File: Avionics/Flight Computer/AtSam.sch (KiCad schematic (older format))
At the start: 41 parts, among them U12 ATSAME70Q21A-AN, Y1 9HT11-32.768KDZB-T, Y2 7V-16.000MAHJ-T

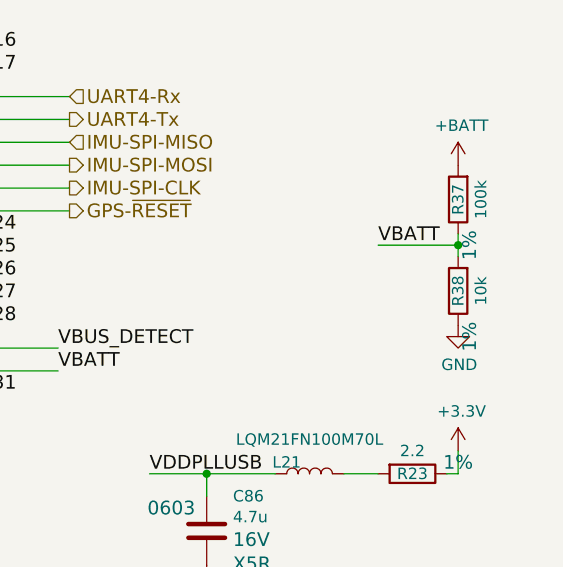
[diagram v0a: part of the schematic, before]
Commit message: Continuing to route out MCU signals.
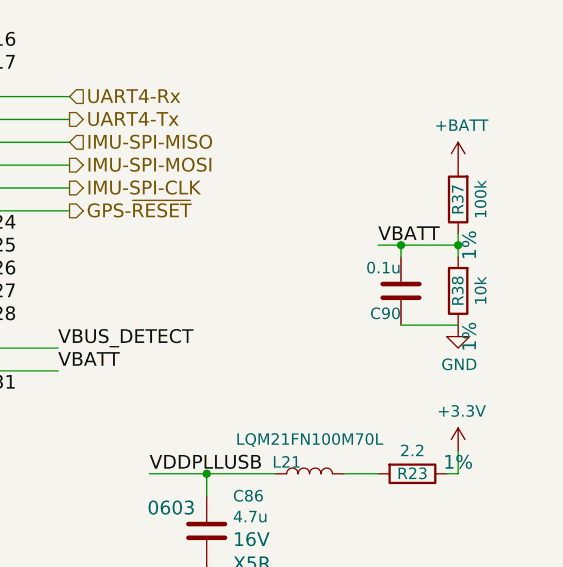
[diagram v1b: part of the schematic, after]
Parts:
- added C90: 0.1u, Capacitors_SMD:C_0402, symbol C
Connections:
- net GND: now also C90.2
- net VBATT: now also C90.1
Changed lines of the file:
@@
 	10850 3900 10850 4000
 Connection ~ 10850 3950
+$Comp
+L C C90
+U 1 1 58BBD62D
+P 10600 4150
+F 0 "C90" H 10600 4050 50  0000 R CNN
+F 1 "0.1u" H 10600 4250 50  0000 R CNN
+F 2 "Capacitors_SMD:C_0402" H 5888 2700 50  0001 C CNN
+F 3 "" H 5850 2850 50  0001 C CNN
+F 4 "50V" H 10485 4188 60  0001 R CNN "Voltage"
+F 5 "20%" H 10715 4006 60  0001 L CNN "Tolerance"
+F 6 "X7R" H 10485 4294 60  0001 R CNN "Type"
+F 7 "0402" H 10715 3953 60  0001 L CNN "Package"
+	1    10600 4150
+	1    0    0    -1
+$EndComp
+Wire Wire Line
+	10600 4000 10600 3950
+Connection ~ 10600 3950
+Wire Wire Line
+	10600 4300 10850 4300
 $EndSCHEMATC

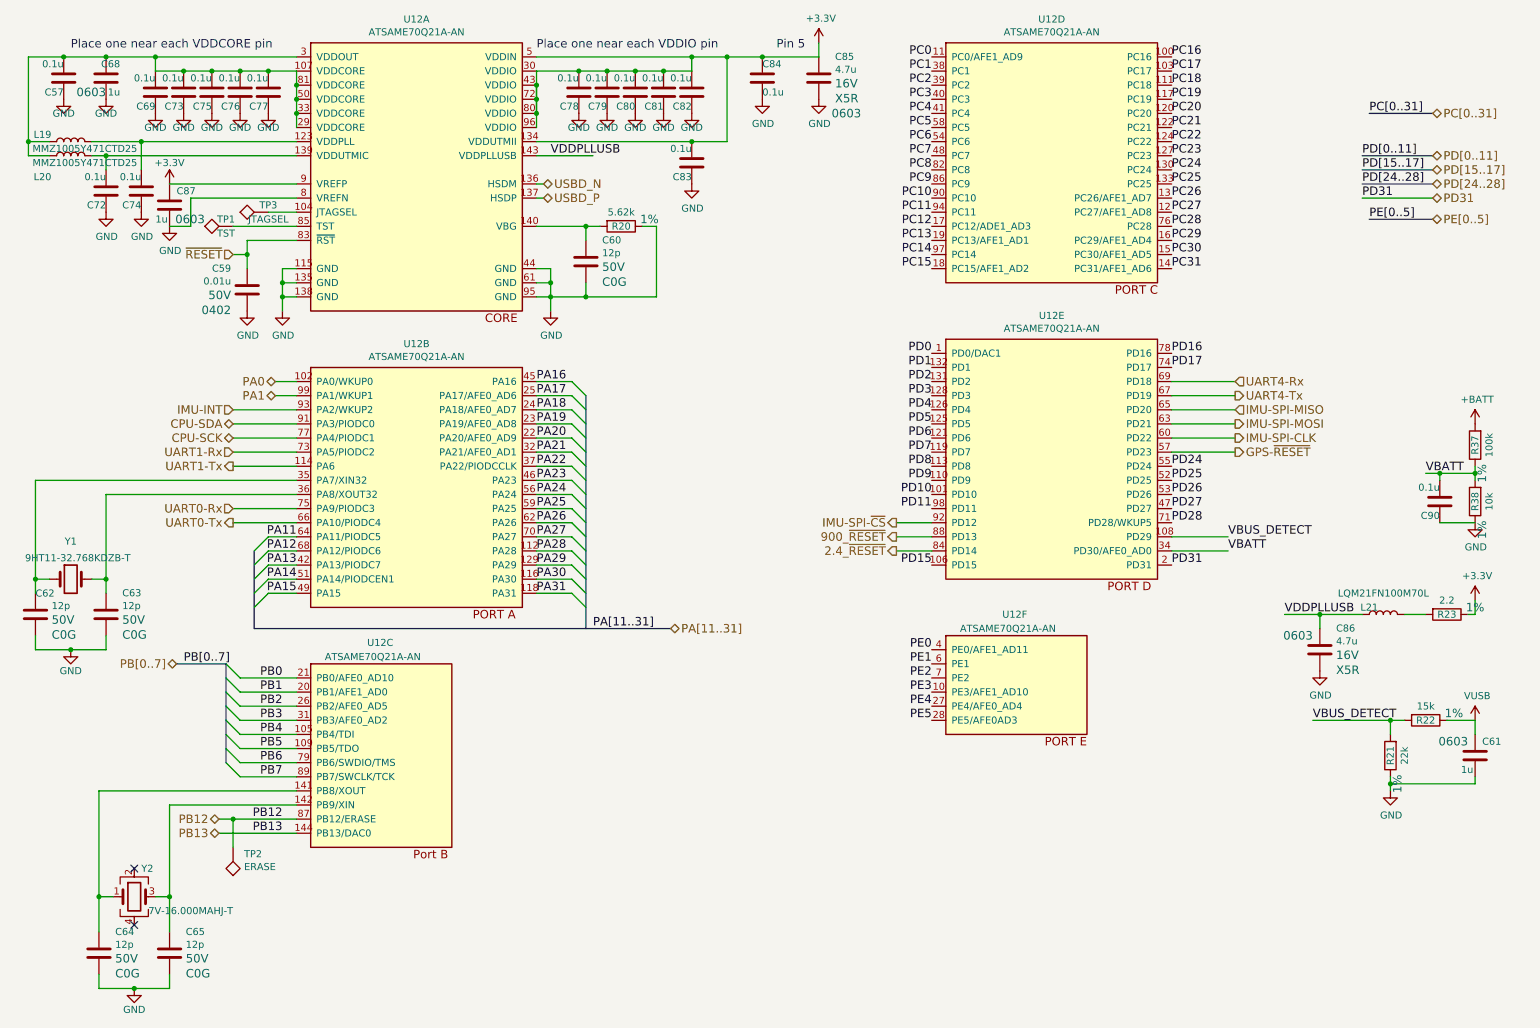
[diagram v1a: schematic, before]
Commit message: Finished routing and DRC check.
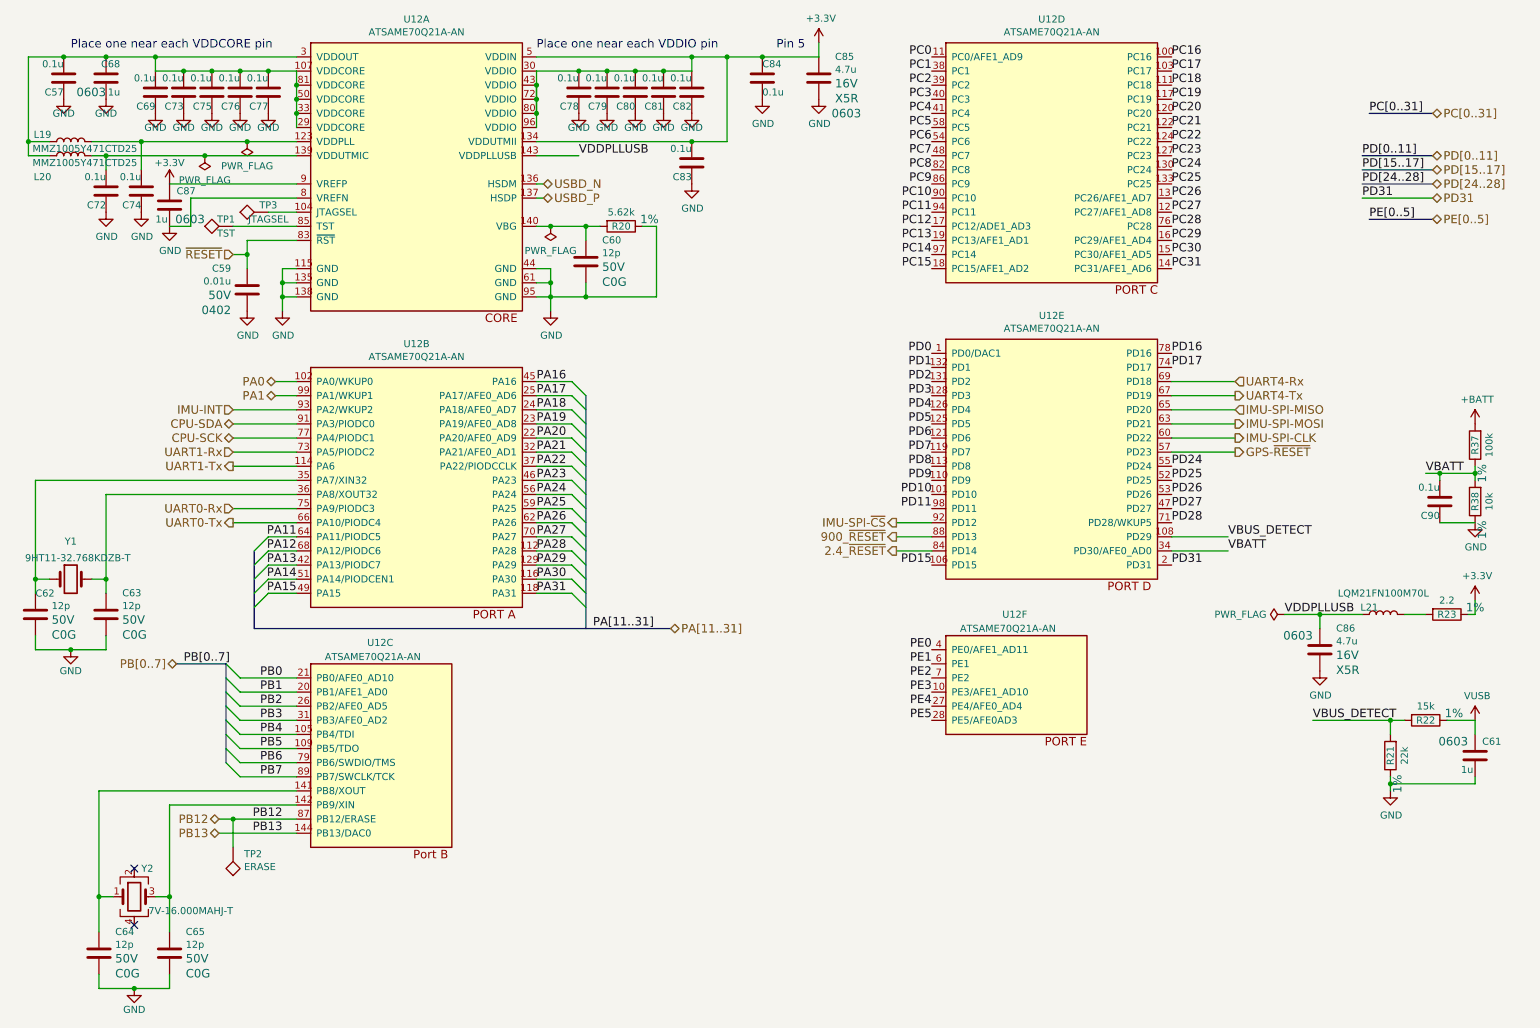
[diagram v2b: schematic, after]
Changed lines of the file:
@@
 USBD_P
 Wire Wire Line
-	4200 1700 4600 1700
-Text Label 4300 1700 0    60   ~ 0
+	4200 1700 4500 1700
+Text Label 4500 1700 0    60   ~ 0
 VDDPLLUSB
 Text Label 9500 4950 0    60   ~ 0
@@
 Wire Wire Line
 	10600 4300 10850 4300
+$Comp
+L PWR_FLAG #FLG034
+U 1 1 58BDE6E5
+P 1850 1700
+F 0 "#FLG034" H -3950 -525 50  0001 C CNN
+F 1 "PWR_FLAG" H 1850 1873 50  0000 C CNN
+F 2 "" H -3950 -600 50  0001 C CNN
+F 3 "" H -3950 -600 50  0001 C CNN
+	1    1850 1700
+	-1   0    0    1
+$EndComp
+$Comp
+L PWR_FLAG #FLG035
+U 1 1 58BDE982
+P 2150 1600
+F 0 "#FLG035" H -3650 -625 50  0001 C CNN
+F 1 "PWR_FLAG" H 2150 1773 50  0000 C CNN
+F 2 "" H -3650 -700 50  0001 C CNN
+F 3 "" H -3650 -700 50  0001 C CNN
+	1    2150 1600
+	-1   0    0    1
+$EndComp
+Connection ~ 1850 1700
+Connection ~ 2150 1600
+$Comp
+L PWR_FLAG #FLG036
+U 1 1 58BDFB15
+P 4300 2200
+F 0 "#FLG036" H -1500 -25 50  0001 C CNN
+F 1 "PWR_FLAG" H 4300 2373 50  0000 C CNN
+F 2 "" H -1500 -100 50  0001 C CNN
+F 3 "" H -1500 -100 50  0001 C CNN
+	1    4300 2200
+	-1   0    0    1
+$EndComp
+Connection ~ 4300 2200
+$Comp
+L PWR_FLAG #FLG037
+U 1 1 58BE124C
+P 9500 4950
+F 0 "#FLG037" H 3700 2725 50  0001 C CNN
+F 1 "PWR_FLAG" V 9500 5078 50  0000 L CNN
+F 2 "" H 3700 2650 50  0001 C CNN
+F 3 "" H 3700 2650 50  0001 C CNN
+	1    9500 4950
+	0    -1   -1   0
+$EndComp
 $EndSCHEMATC

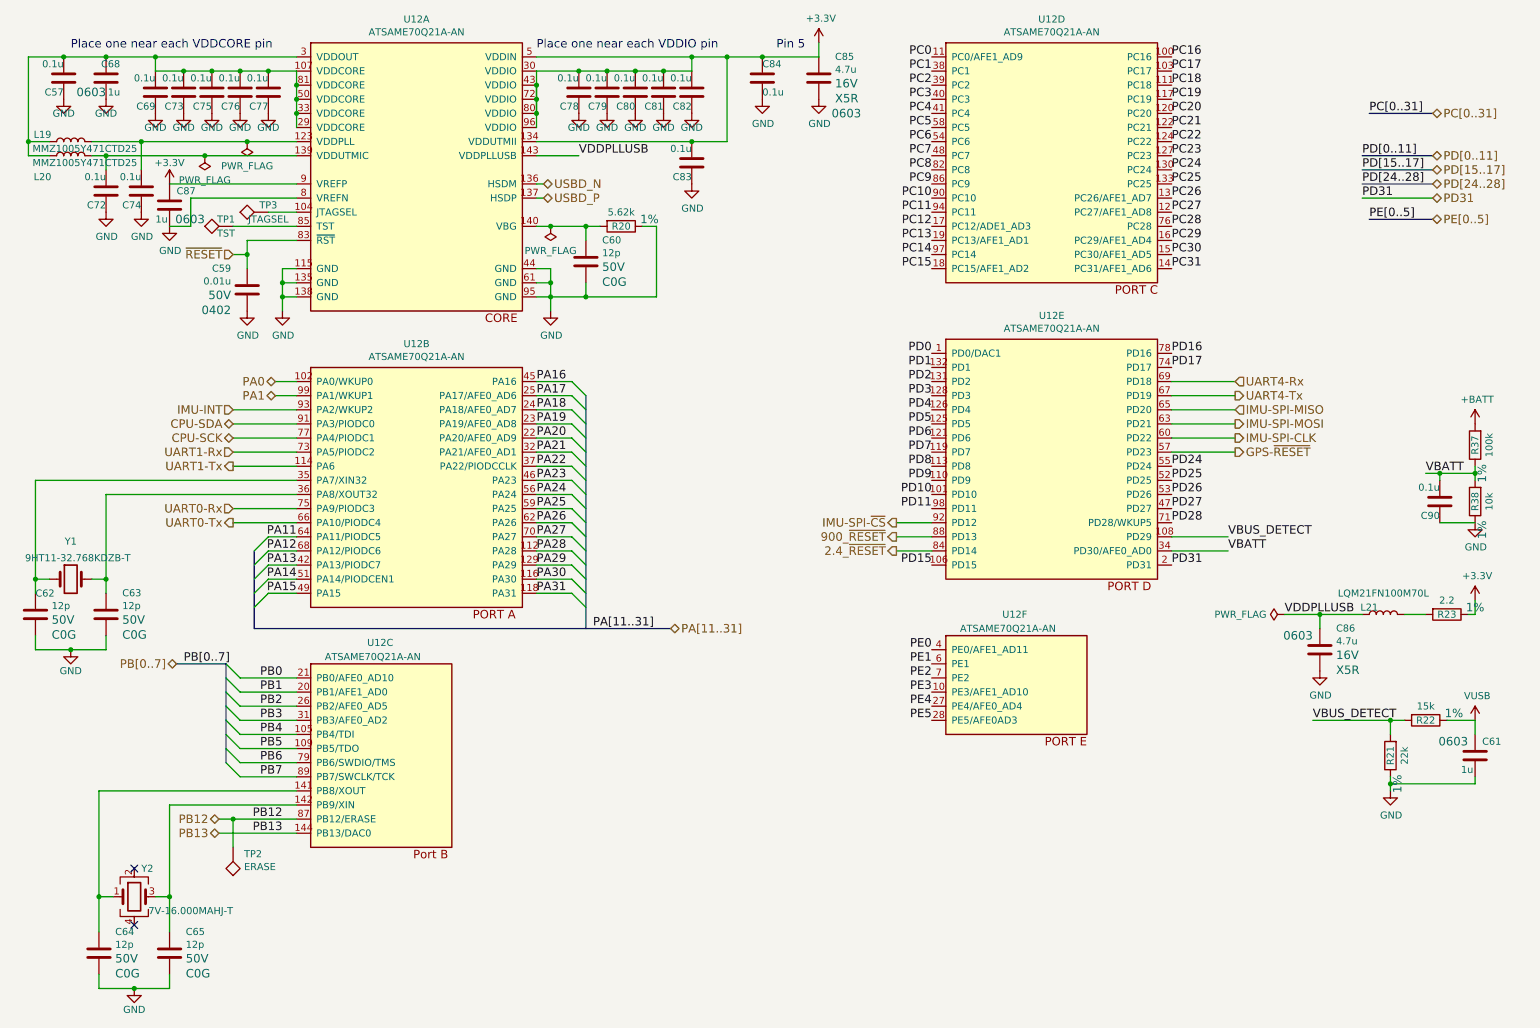
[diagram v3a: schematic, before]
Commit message: Changed LED configuration, added smart driver chip to let all the CPUs access it..
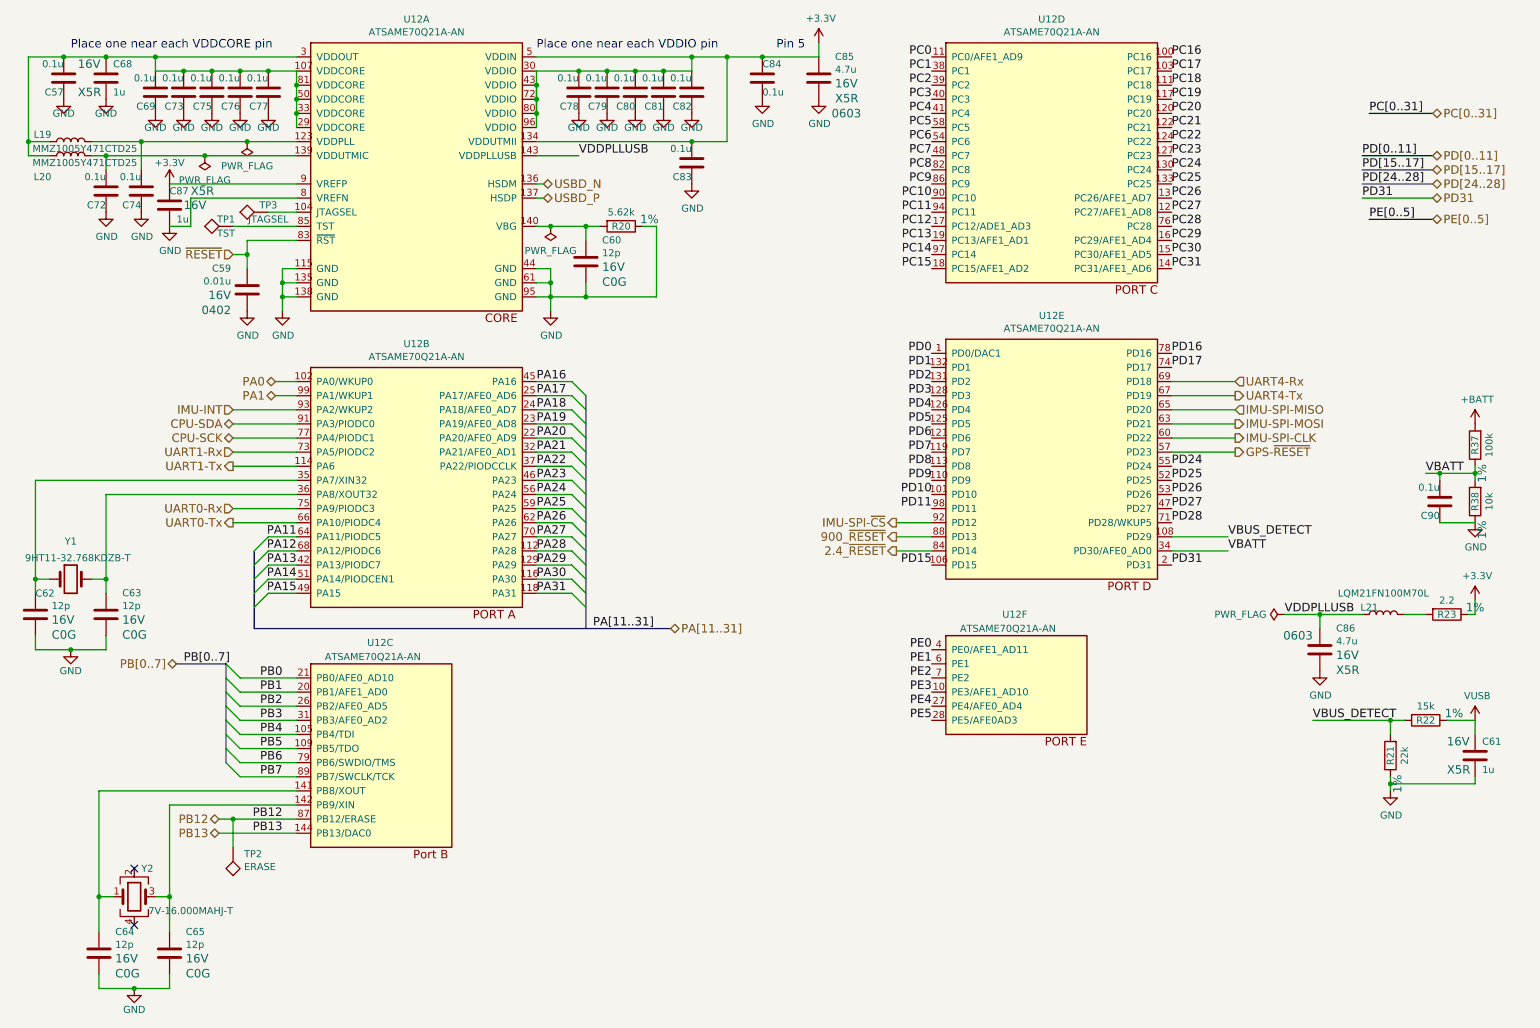
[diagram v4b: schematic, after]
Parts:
- C57, C59, C60, C62, C63, C64, C65, C69, C72, C73, C74, C75, C76, C77, C78, C79, C80, C81, C82, C83, C84, C90, R20, R21, R22, R23: Voltage 50V -> 16V
- C61, C68, C87: footprint Capacitors_SMD:C_0603 -> Capacitors_SMD:C_0402; Package 0603 -> 0402; Type X7R -> X5R; Voltage 50V -> 16V
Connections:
- net +3V3: now also C87.1; no longer C87.2
- net GND: now also C61.2, C68.2, C87.2; no longer C61.1, C68.1, C87.1
- net VUSB: now also C61.1; no longer C61.2
- net at C57.1, C69.1, C73.1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: now also C68.1; no longer C68.2
